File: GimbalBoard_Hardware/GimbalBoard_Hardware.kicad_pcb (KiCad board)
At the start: 2 copper layers, 124 x 76.2 mm, 1 part, among them U5 Teensy4.1_DEV-16771

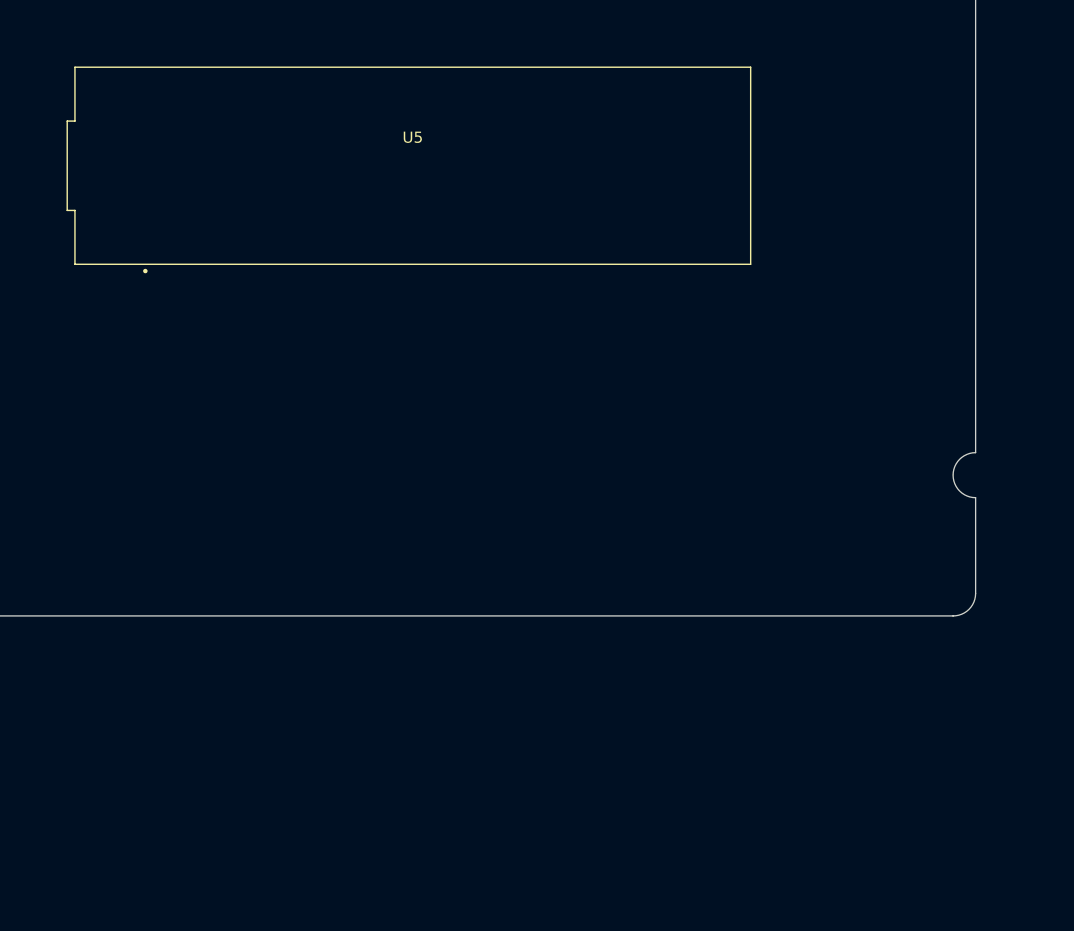
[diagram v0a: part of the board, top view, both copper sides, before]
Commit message: moved footprints
I moved some footprints around and asked some questions about trace width. as well as fixed the ethernet cap footprint
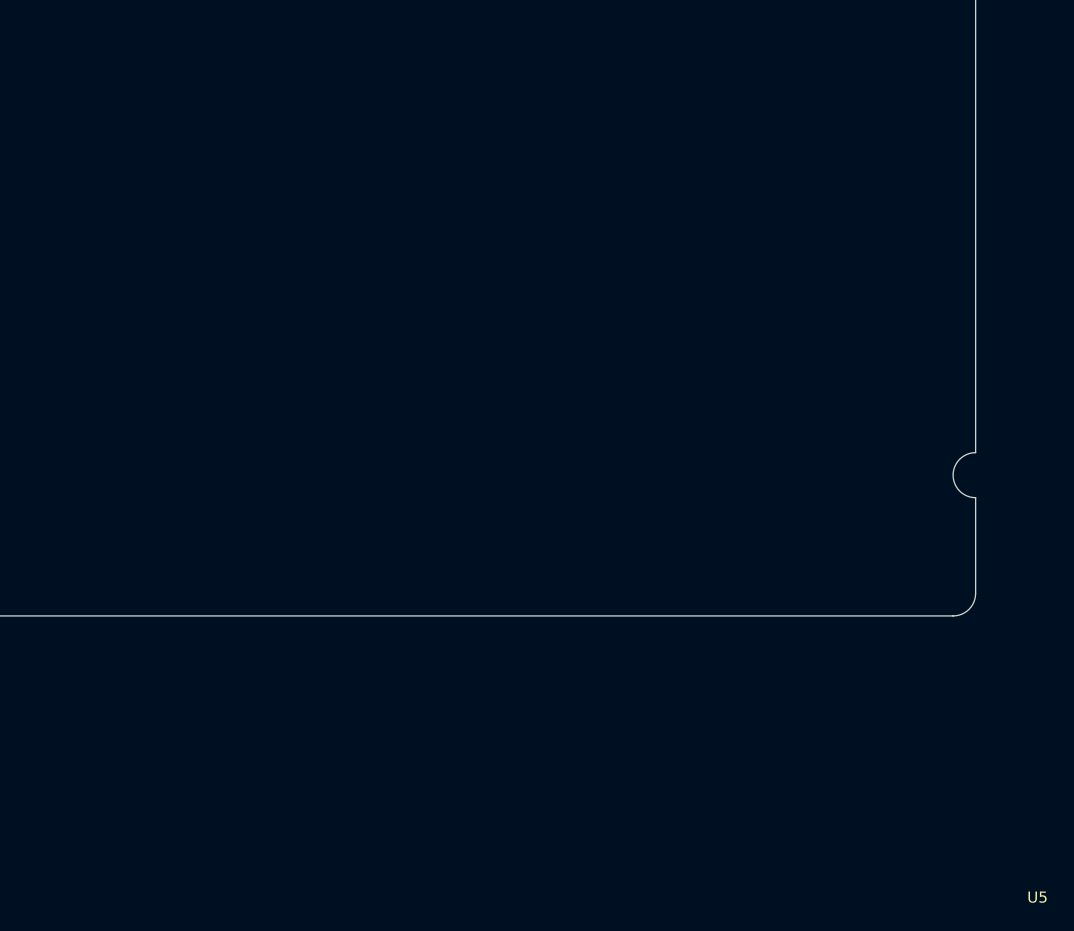
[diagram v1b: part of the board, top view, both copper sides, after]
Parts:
- moved U5 88.8 mm to (103.6, 113.3)

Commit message: some changes
added half an inch to the board and some other shit
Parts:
- moved U5 223.6 mm to (321.6, 63.4)
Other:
- board size 124 x 76.2 mm -> 124 x 74.2 mm
